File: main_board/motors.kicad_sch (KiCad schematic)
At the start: 18 parts

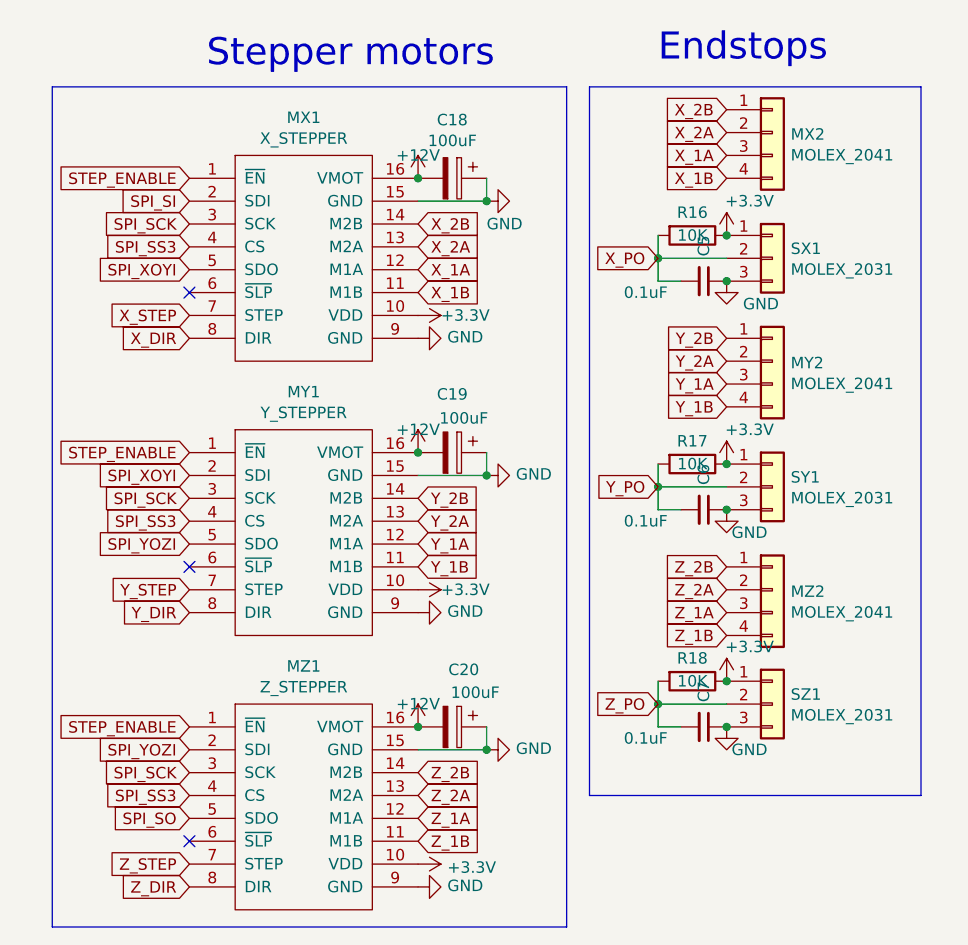
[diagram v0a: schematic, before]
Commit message: updated step models
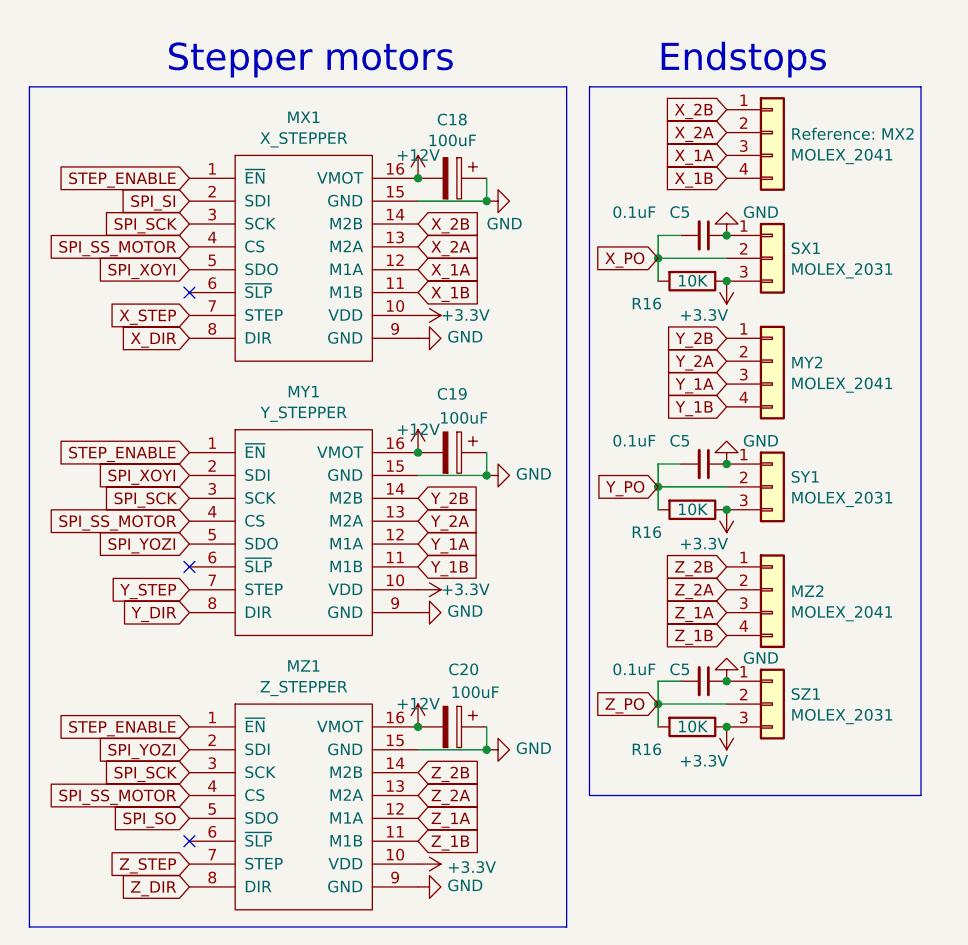
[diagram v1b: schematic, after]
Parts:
- removed C6, C7: 0.1uF, Capacitor_SMD:C_0805_2012Metric_Pad1.18x1.45mm_HandSolder, symbol Device:C_Small
- removed R17, R18: 10K, Resistor_SMD:R_0805_2012Metric, symbol Device:R
- added C5 (x2): 0.1uF, Capacitor_SMD:C_0805_2012Metric_Pad1.18x1.45mm_HandSolder, symbol Device:C_Small
- added R16 (x2): 10K, Resistor_SMD:R_0805_2012Metric, symbol Device:R
- MX2, MY2, MZ2: footprint Connector_PinHeader_2.54mm:PinHeader_1x04_P2.54mm_Vertical -> Connector_PinHeader_2.54mm:PinHeader_1x04_P2.54mm_Horizontal
- SX1, SY1, SZ1: footprint Connector_PinHeader_2.54mm:PinHeader_1x03_P2.54mm_Vertical -> Connector_PinHeader_2.54mm:PinHeader_1x03_P2.54mm_Horizontal
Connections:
- net +3.3V: now also SX1.3 (Pin_3), SY1.3 (Pin_3), SZ1.3 (Pin_3), R16.1, R16.1; no longer SX1.1 (Pin_1), SY1.1 (Pin_1), SZ1.1 (Pin_1)
- net GND: now also SX1.1 (Pin_1), SY1.1 (Pin_1), SZ1.1 (Pin_1), C5.1, C5.1; no longer SX1.3 (Pin_3), SY1.3 (Pin_3), SZ1.3 (Pin_3)
- net Y_PO: now also C5.2, R16.2
- net Z_PO: now also C5.2, R16.2
- net SPI_SS3 renamed SPI_SS_MOTOR
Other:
- moved on the sheet: C5, R16

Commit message: routed main board
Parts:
- C18, C19, C20: footprint Capacitor_THT:CP_Radial_D6.3mm_P2.50mm -> footprints:CP_Radial_D6.3mm_P2.50mm
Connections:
- net X_1A: now also MX2.2 (Pin_2); no longer MX2.3 (Pin_3)
- net X_1B: now also MX2.1 (Pin_1); no longer MX2.4 (Pin_4)
- net X_2A: now also MX2.3 (Pin_3); no longer MX2.2 (Pin_2)
- net X_2B: now also MX2.4 (Pin_4); no longer MX2.1 (Pin_1)
- net Y_1A: now also MY2.2 (Pin_2); no longer MY2.3 (Pin_3)
- net Y_1B: now also MY2.1 (Pin_1); no longer MY2.4 (Pin_4)
- net Y_2A: now also MY2.3 (Pin_3); no longer MY2.2 (Pin_2)
- net Y_2B: now also MY2.4 (Pin_4); no longer MY2.1 (Pin_1)
- net Z_1A: now also MZ2.2 (Pin_2); no longer MZ2.3 (Pin_3)
- net Z_1B: now also MZ2.1 (Pin_1); no longer MZ2.4 (Pin_4)
- net Z_2A: now also MZ2.3 (Pin_3); no longer MZ2.2 (Pin_2)
- net Z_2B: now also MZ2.4 (Pin_4); no longer MZ2.1 (Pin_1)
